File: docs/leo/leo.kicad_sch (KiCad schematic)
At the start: 21 parts, among them IC11 GAL16V8, IC20 74153, IC21 74LS273, IC29 74LS273, IC37 MB81C78A, IC38 MB81C78A, IC40 74LS04, IC41 GAL16V8, IC51 GAL16V8, IC52 74LS32, IC56 74LS245, IC57 74LS245, IC58 74LS244, IC59 74LS244, IC60 74LS244, IC61 74LS139, IC62 74LS20, IC8 7486

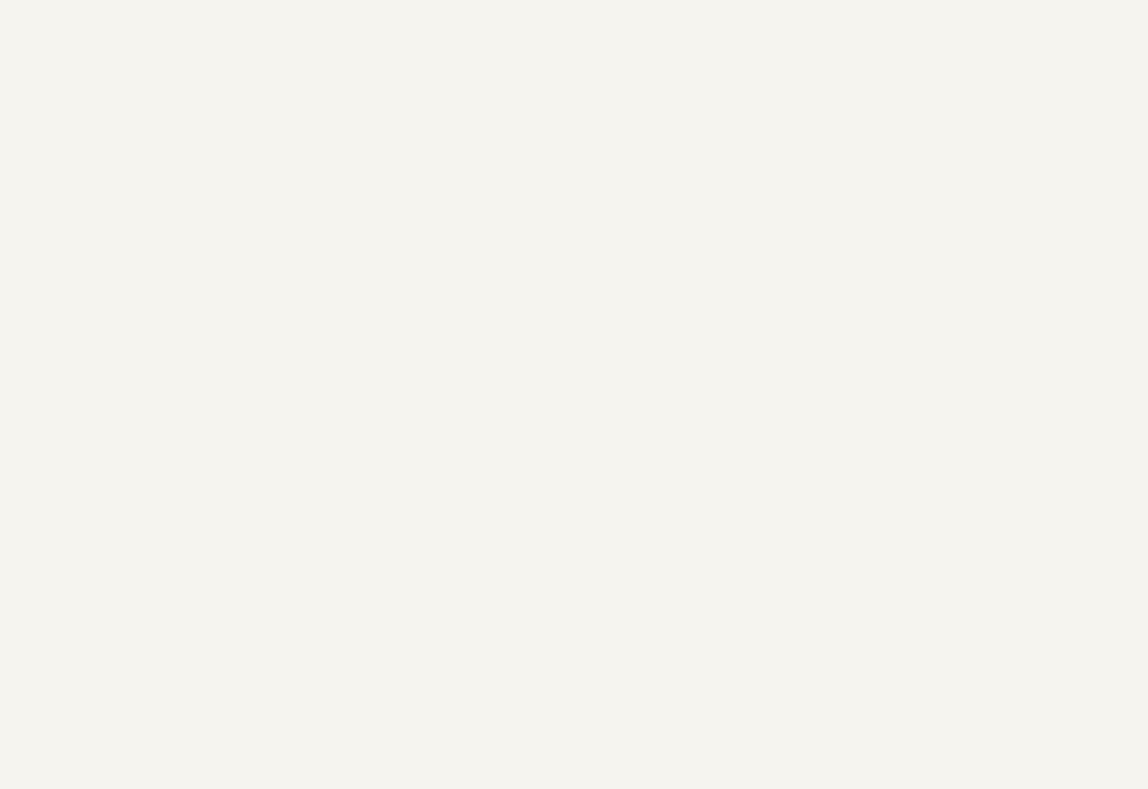
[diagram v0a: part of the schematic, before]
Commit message: Split bank switching into its own sheet
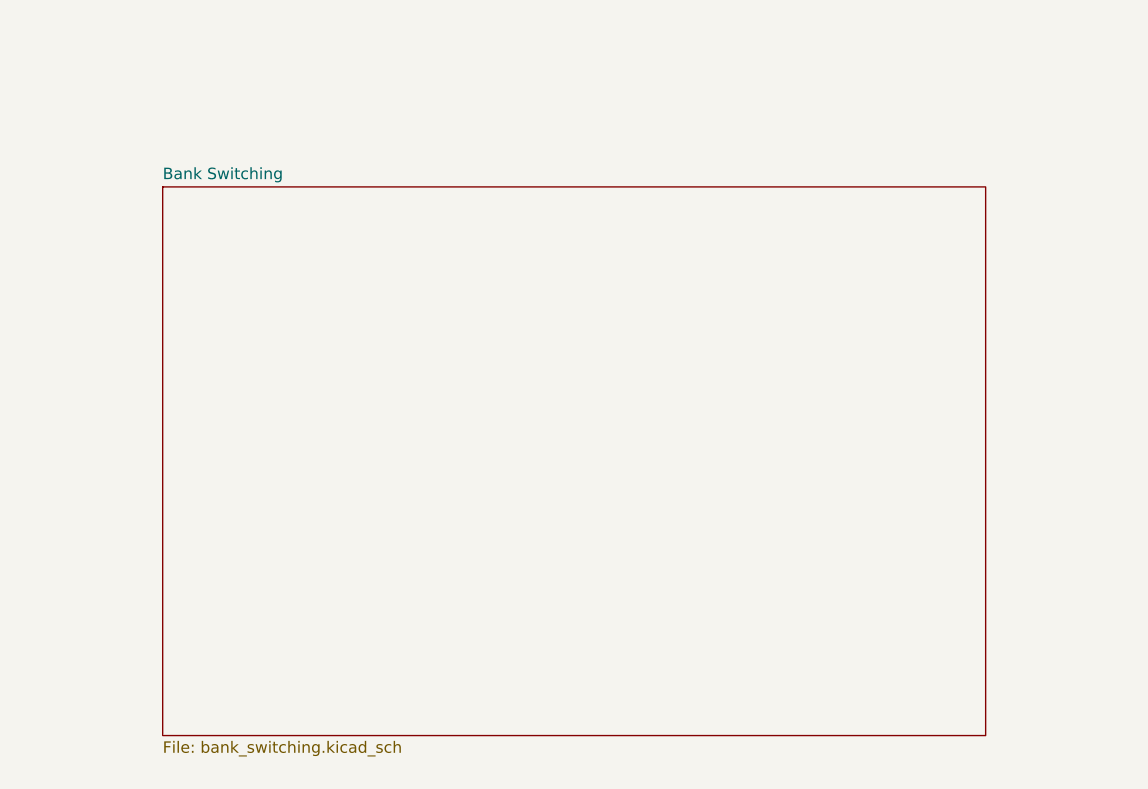
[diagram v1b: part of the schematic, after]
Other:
- added sheet Bank Switching (bank_switching.kicad_sch)
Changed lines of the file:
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@@
+    )
+  )
+  (sheet (at 384.81 727.71) (size 91.44 60.96) (fields_autoplaced)
+    (stroke (width 0.1524) (type solid) (color 0 0 0 0))
+    (fill (color 0 0 0 0.0000))
+    (property "Sheet name" "Bank Switching" (id 0) (at 384.81 726.9984 0)
+      (effects (font (size 1.27 1.27)) (justify left bottom))
+    )
+    (property "Sheet file" "bank_switching.kicad_sch" (id 1) (at 384.81 789.2546 0)
+      (effects (font (size 1.27 1.27)) (justify left top))
     )
   )
@@
     (path "/95da80d1-f524-4dae-9bdb-cc834e22a0a6" (page "8"))
     (path "/179d7767-9223-42a1-9464-f2f519087c7e" (page "9"))
+    (path "/a247e571-a252-4b17-b29c-33153965b7ae" (page "10"))
   )
   (symbol_instances
@@
       (reference "#PWR?") (unit 1) (value "VCC") (footprint "")
     )
+    (path "/a247e571-a252-4b17-b29c-33153965b7ae/a3719e5c-576f-4695-ab5a-602a06fbbb7d"
+      (reference "#PWR?") (unit 1) (value "VCC") (footprint "")
+    )
     (path "/3f170781-d744-477d-adf1-ed36cff99e11/bb643d94-c0fc-4900-87e8-52fdcfa2623a"
       (reference "#PWR?") (unit 1) (value "GND") (footprint "")
@@
     (path "/179d7767-9223-42a1-9464-f2f519087c7e/beb61fd4-017a-4806-b8de-53b203a2a546"
       (reference "#PWR?") (unit 1) (value "VCC") (footprint "")
+    )
+    (path "/a247e571-a252-4b17-b29c-33153965b7ae/bef1a978-183f-466d-9f9e-5959f87a8db5"
+      (reference "#PWR?") (unit 1) (value "GND") (footprint "")
     )
     (path "/3f170781-d744-477d-adf1-ed36cff99e11/c7de3329-b4e8-4d45-a030-6104281a2e4a"
@@
       (reference "IC28") (unit 1) (value "74153") (footprint "")
     )
-    (path "/179d7767-9223-42a1-9464-f2f519087c7e/80a98361-1417-4d31-b88a-253c2c6fff83"
+    (path "/a247e571-a252-4b17-b29c-33153965b7ae/80a98361-1417-4d31-b88a-253c2c6fff83"
       (reference "IC28") (unit 1) (value "74LS138") (footprint "")
     )
@@
       (reference "IC31") (unit 1) (value "74LS374") (footprint "")
     )
-    (path "/179d7767-9223-42a1-9464-f2f519087c7e/4c91eaa6-f6d2-4815-8cde-e92e109c05a9"
+    (path "/a247e571-a252-4b17-b29c-33153965b7ae/4c91eaa6-f6d2-4815-8cde-e92e109c05a9"
       (reference "IC35") (unit 1) (value "74LS175") (footprint "")
     )
-    (path "/179d7767-9223-42a1-9464-f2f519087c7e/a7e426fa-892b-4004-b7ff-4f56096c99b6"
+    (path "/a247e571-a252-4b17-b29c-33153965b7ae/a7e426fa-892b-4004-b7ff-4f56096c99b6"
       (reference "IC36") (unit 1) (value "74LS157") (footprint "")
     )
@@
       (reference "IC63") (unit 1) (value "GA22") (footprint "")
     )
-    (path "/179d7767-9223-42a1-9464-f2f519087c7e/41f1ebb1-cb26-42fd-97b2-04e392551d7a"
+    (path "/a247e571-a252-4b17-b29c-33153965b7ae/446f1ba9-c82b-40a0-ba4a-c5ae2e5dc5ff"
+      (reference "J16") (unit 1) (value "Jumper_3_Open") (footprint "")
+    )
+    (path "/a247e571-a252-4b17-b29c-33153965b7ae/41f1ebb1-cb26-42fd-97b2-04e392551d7a"
       (reference "J20") (unit 1) (value "Jumper_3_Bridged12") (footprint "")
     )

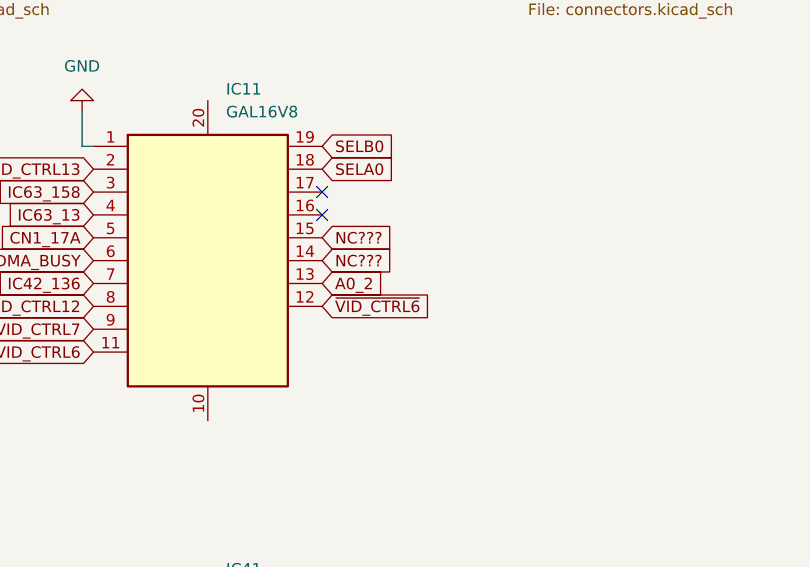
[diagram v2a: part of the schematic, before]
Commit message: Name video control bits Correct palette addressing
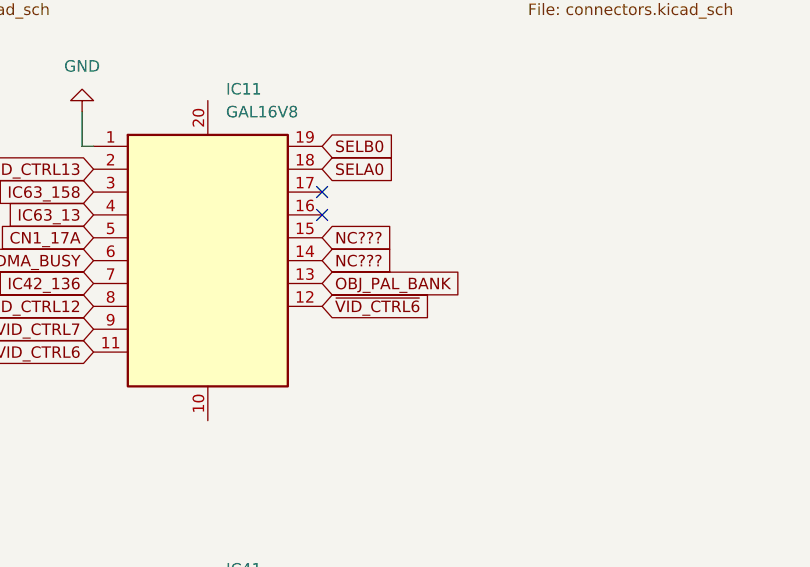
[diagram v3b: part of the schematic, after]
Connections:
- net A0_2 renamed OBJ_PAL_BANK
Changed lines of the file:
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@@
     )
   )
-  (global_label "A0_2" (shape input) (at 182.88 120.65 0) (fields_autoplaced)
+  (global_label "OBJ_PAL_BANK" (shape input) (at 182.88 120.65 0) (fields_autoplaced)
     (effects (font (size 1.27 1.27)) (justify left))
-    (property "Intersheet References" "${INTERSHEET_REFS}" (id 0) (at 189.7683 120.7294 0)
+    (property "Intersheet References" "${INTERSHEET_REFS}" (id 0) (at 199.1421 120.5706 0)
       (effects (font (size 1.27 1.27)) (justify left) hide)
     )

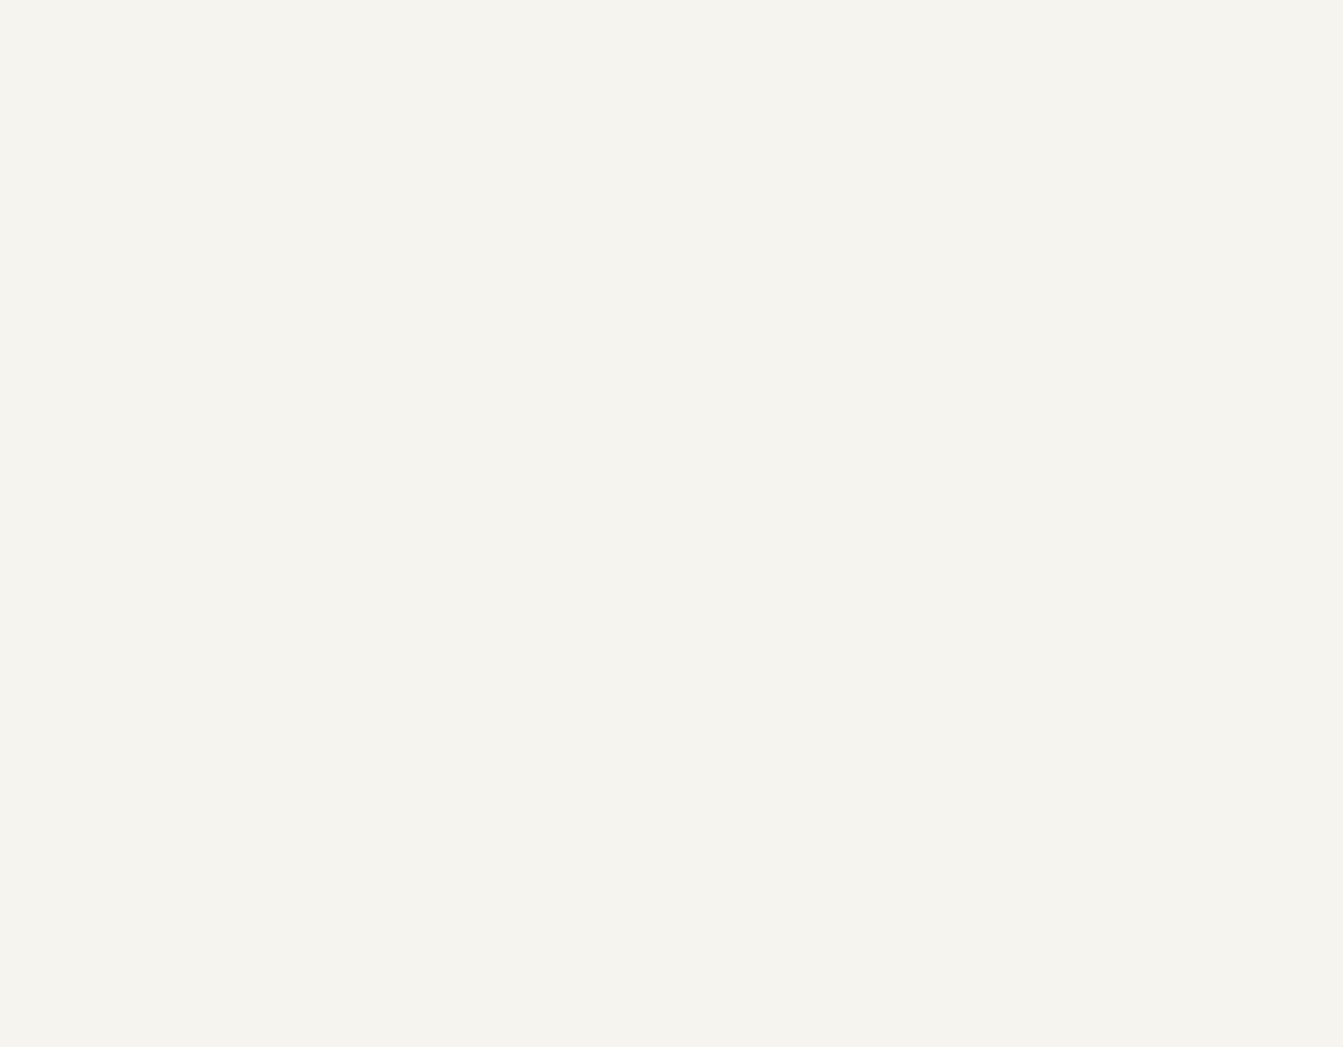
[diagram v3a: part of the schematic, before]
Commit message: Added ga20 sample channel filters
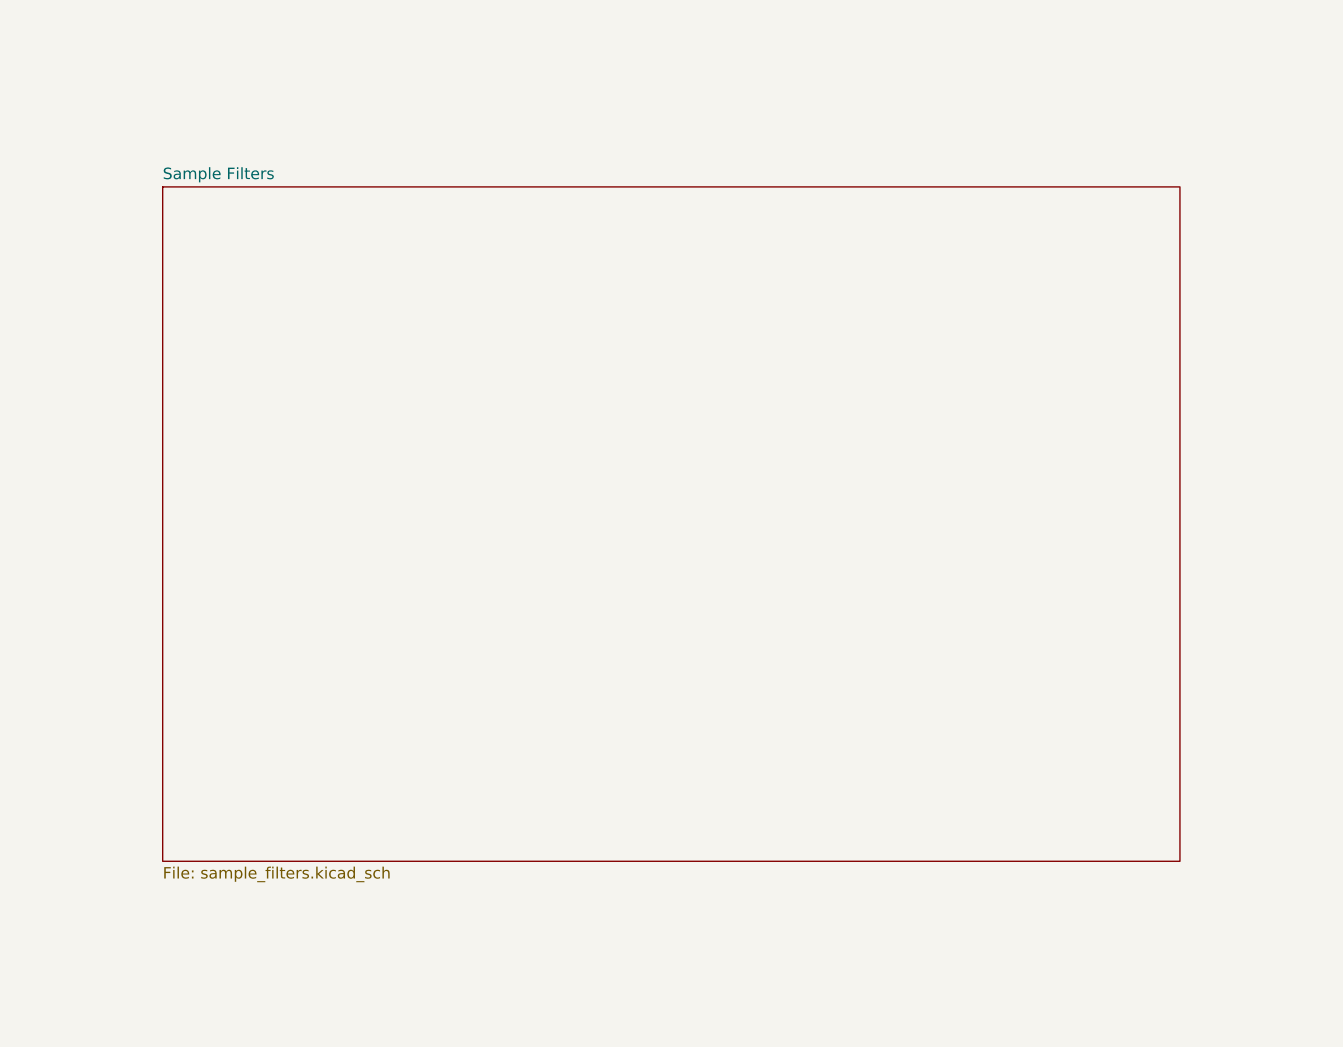
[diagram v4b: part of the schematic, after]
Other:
- added sheet Sample Filters (sample_filters.kicad_sch)

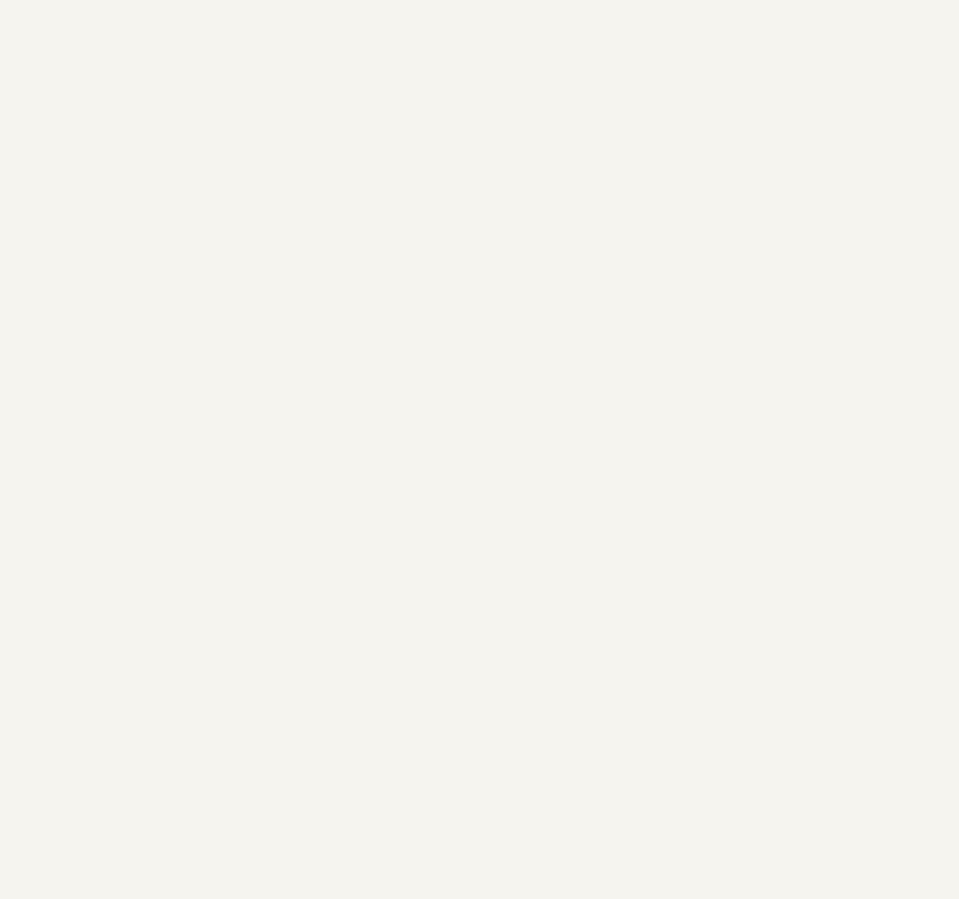
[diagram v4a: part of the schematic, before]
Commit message: Map out most of audio cpu
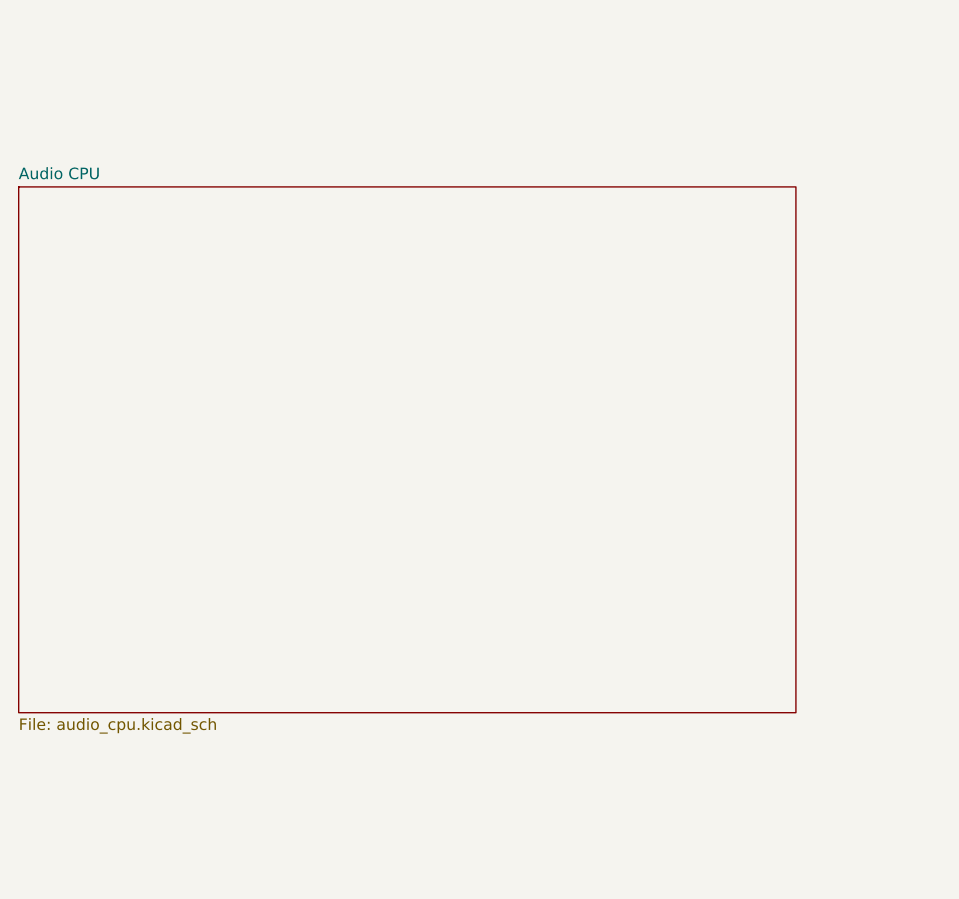
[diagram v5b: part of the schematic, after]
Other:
- added sheet Audio CPU (audio_cpu.kicad_sch)
